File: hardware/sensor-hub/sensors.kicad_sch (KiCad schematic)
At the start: 7 parts, among them U5 SCD40-D-R2, U6 SHT4x, U7 LPS22HH

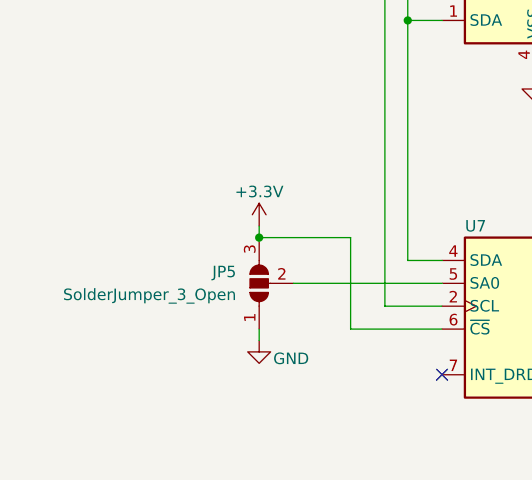
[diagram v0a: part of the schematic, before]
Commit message: Change crystal packages, assign footprints
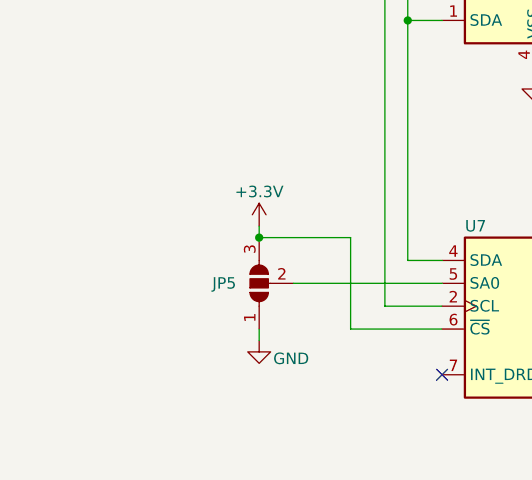
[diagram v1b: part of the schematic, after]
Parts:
- C33, C34, C35: footprint (none) -> Capacitor_SMD:C_0603_1608Metric
- JP5: footprint (none) -> Jumper:SolderJumper-3_P1.3mm_Open_RoundedPad1.0x1.5mm
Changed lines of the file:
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@@
 			)
 		)
-		(property "Footprint" ""
+		(property "Footprint" "Capacitor_SMD:C_0603_1608Metric"
 			(at 152.4 82.55 0)
 			(effects
@@
 		(fields_autoplaced yes)
 		(property "Reference" "JP5"
-			(at 107.95 118.1099 90)
+			(at 107.95 119.3799 90)
 			(effects
 				(font
@@
 				)
 				(justify left)
-			)
-		)
-		(property "Footprint" ""
+				(hide yes)
+			)
+		)
+		(property "Footprint" "Jumper:SolderJumper-3_P1.3mm_Open_RoundedPad1.0x1.5mm"
 			(at 110.49 119.38 0)
 			(effects
@@
 			)
 		)
-		(property "Footprint" ""
+		(property "Footprint" "Capacitor_SMD:C_0603_1608Metric"
 			(at 152.4 57.15 0)
 			(effects
@@
 			)
 		)
-		(property "Footprint" ""
+		(property "Footprint" "Capacitor_SMD:C_0603_1608Metric"
 			(at 158.75 111.76 0)
 			(effects

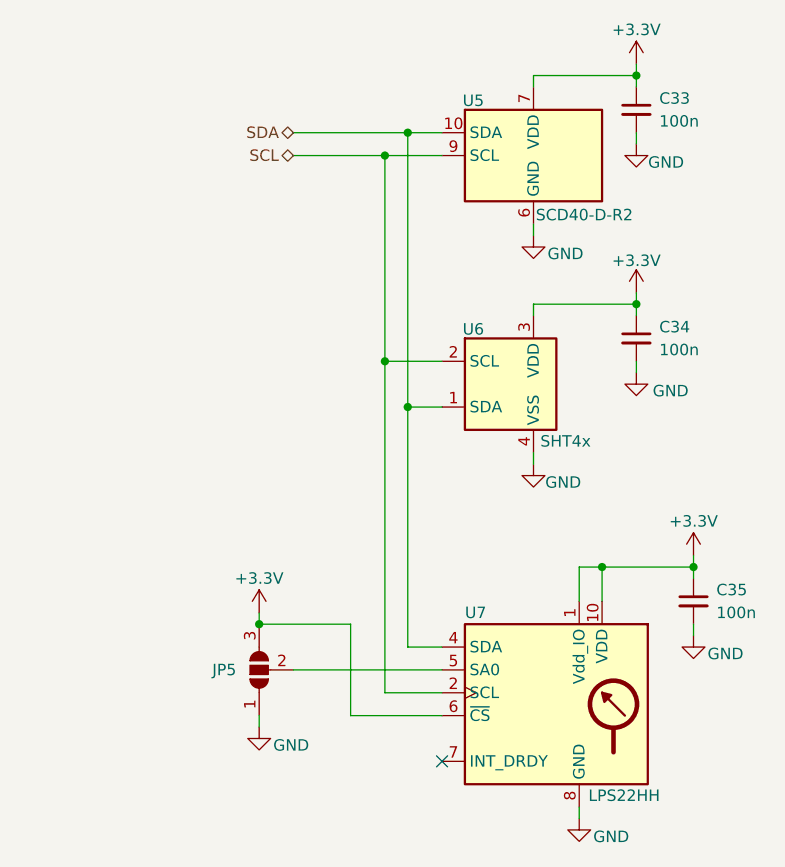
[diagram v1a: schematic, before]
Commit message: Assign remaining footprints, change HT sensor
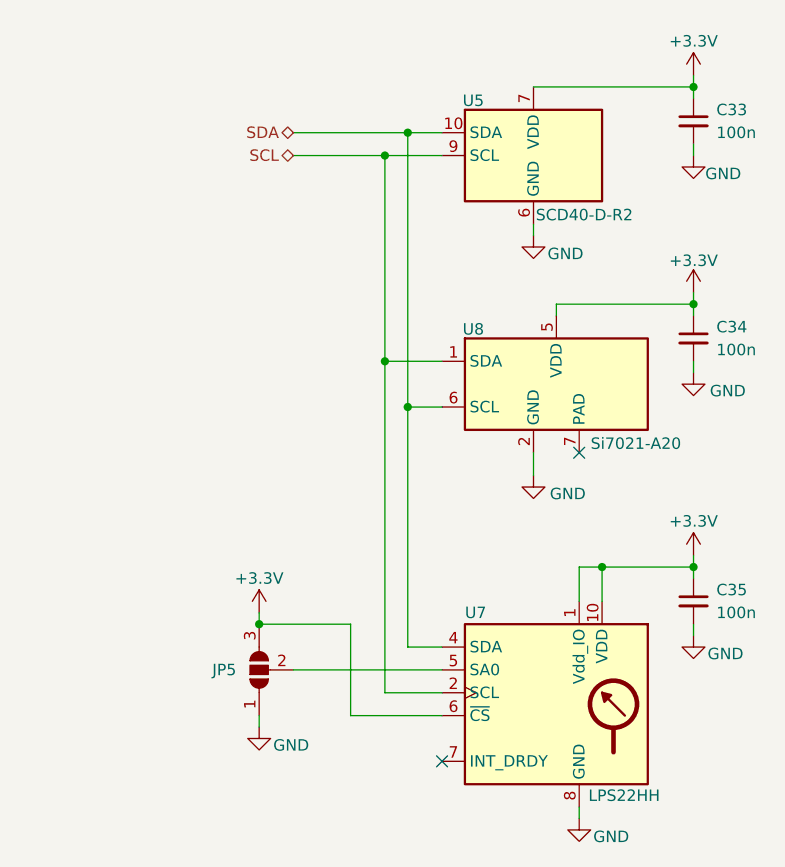
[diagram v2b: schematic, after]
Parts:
- removed U6: SHT4x, Sensor_Humidity:Sensirion_DFN-4_1.5x1.5mm_P0.8mm_SHT4x_NoCentralPad, symbol Sensor_Humidity:SHT4x
- added U8: Si7021-A20, Package_DFN_QFN:DFN-6-1EP_3x3mm_P1mm_EP1.5x2.4mm, symbol Sensor_Humidity:Si7021-A20
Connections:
- net +3.3V: now also U8.5 (VDD)
- net GND: now also U8.2 (GND)
- net SCL: now also U8.1 (SDA)
- net SDA: now also U8.6 (SCL)
- no-connect marks 1 -> 2
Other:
- moved on the sheet: C33, C34

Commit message: Finalize layout
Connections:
- net SCL: now also U8.6 (SCL); no longer U8.1 (SDA)
- net SDA: now also U8.1 (SDA); no longer U8.6 (SCL)
- net +3.3V renamed +3.3V_LDO
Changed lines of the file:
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@@
+	)
+	(junction
+		(at 127 85.09)
+		(diameter 0)
+		(color 0 0 0 0)
 	)
 	(junction
@@
 	)
 	(junction
-		(at 127 90.17)
-		(diameter 0)
-		(color 0 0 0 0)
-	)
-	(junction
-		(at 124.46 85.09)
+		(at 124.46 90.17)
 		(diameter 0)
 		(color 0 0 0 0)
@@
 	(wire
 		(pts
-			(xy 127 90.17) (xy 130.81 90.17)
+			(xy 127 85.09) (xy 130.81 85.09)
 		)
 		(stroke
@@
 	(wire
 		(pts
+			(xy 127 85.09) (xy 127 116.84)
+		)
+		(stroke
+			(width 0)
+			(type default)
+		)
+	)
+	(wire
+		(pts
 			(xy 110.49 124.46) (xy 110.49 125.73)
 		)
@@
 	(wire
 		(pts
-			(xy 124.46 62.23) (xy 124.46 85.09)
+			(xy 124.46 90.17) (xy 124.46 121.92)
+		)
+		(stroke
+			(width 0)
+			(type default)
+		)
+	)
+	(wire
+		(pts
+			(xy 124.46 62.23) (xy 124.46 90.17)
 		)
 		(stroke
@@
 	(wire
 		(pts
-			(xy 124.46 85.09) (xy 130.81 85.09)
-		)
-		(stroke
-			(width 0)
-			(type default)
-		)
-	)
-	(wire
-		(pts
 			(xy 114.3 119.38) (xy 130.81 119.38)
 		)
@@
 	(wire
 		(pts
-			(xy 127 90.17) (xy 127 116.84)
-		)
-		(stroke
-			(width 0)
-			(type default)
-		)
-	)
-	(wire
-		(pts
 			(xy 158.75 114.3) (xy 158.75 115.57)
 		)
@@
 	(wire
 		(pts
-			(xy 124.46 85.09) (xy 124.46 121.92)
-		)
-		(stroke
-			(width 0)
-			(type default)
-		)
-	)
-	(wire
-		(pts
 			(xy 158.75 85.09) (xy 158.75 86.36)
 		)
@@
 	(wire
 		(pts
+			(xy 124.46 90.17) (xy 130.81 90.17)
+		)
+		(stroke
+			(width 0)
+			(type default)
+		)
+	)
+	(wire
+		(pts
 			(xy 158.75 60.96) (xy 158.75 62.23)
 		)
@@
 	(wire
 		(pts
-			(xy 127 59.69) (xy 127 90.17)
+			(xy 127 59.69) (xy 127 85.09)
 		)
 		(stroke
@@
 			)
 		)
-		(property "Value" "+3.3V"
+		(property "Value" "+3.3V_LDO"
 			(at 158.75 73.914 0)
 			(effects
@@
 			)
 		)
-		(property "Value" "+3.3V"
+		(property "Value" "+3.3V_LDO"
 			(at 158.75 102.87 0)
 			(effects
@@
 			)
 		)
-		(property "Value" "+3.3V"
+		(property "Value" "+3.3V_LDO"
 			(at 110.49 109.22 0)
 			(effects
@@
 			)
 		)
-		(property "Value" "+3.3V"
+		(property "Value" "+3.3V_LDO"
 			(at 158.75 49.53 0)
 			(effects
